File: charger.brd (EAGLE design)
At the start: 42 x 13.2 mm, 12 parts

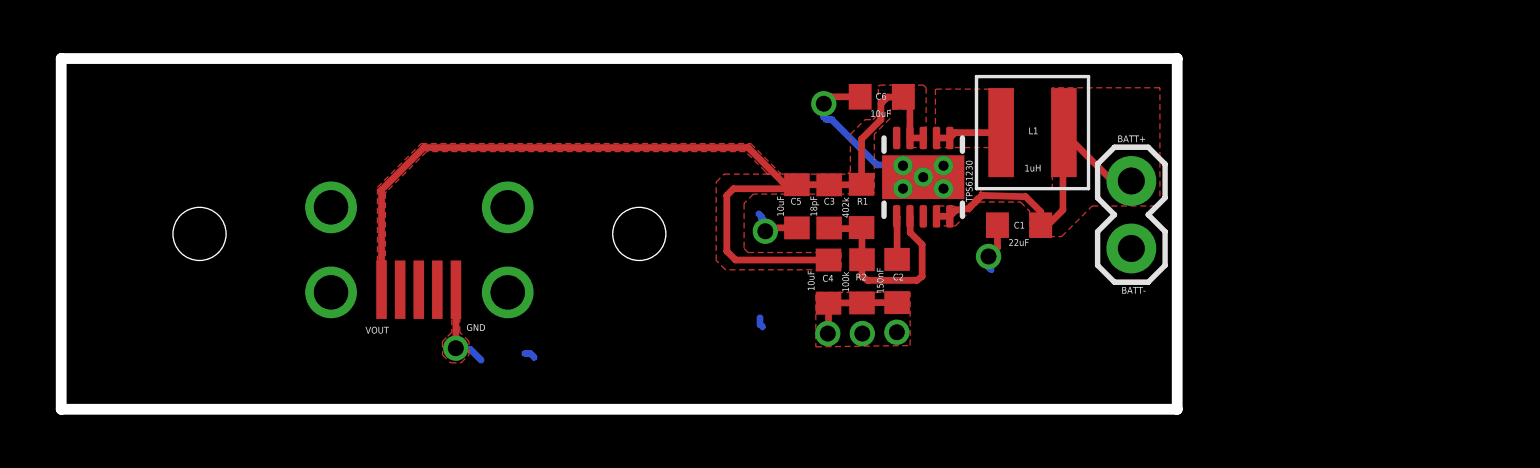
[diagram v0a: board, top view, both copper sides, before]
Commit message: Fixed inductor footprint, updated layout
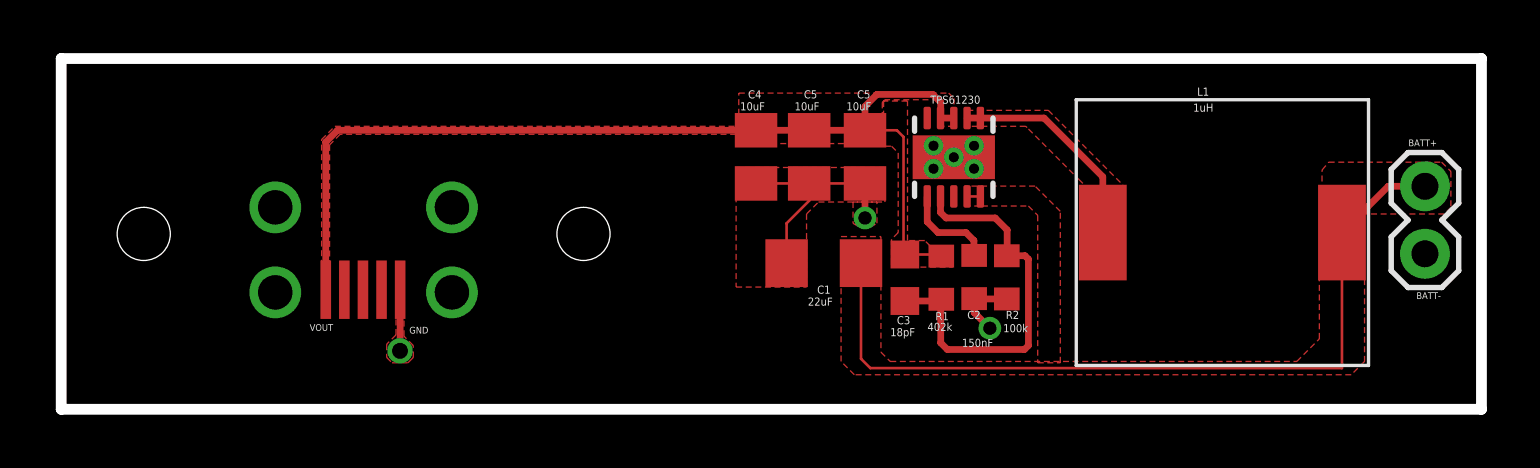
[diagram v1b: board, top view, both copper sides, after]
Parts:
- removed L1: 1uH, Coilcraft:XFL4020
- added U$3: SRU1028, ti:SRU1028
- C1: device adafruit:C0603K -> resistor:C1206
- C3: value 18pF -> 18 pF; device adafruit:C0603K -> resistor:C0603K
- C4, C5, C6: device adafruit:C0603K -> resistor:C0805K
- moved JP1 11.1 mm to (51.3, 5.85)
- moved C1 7.49 mm to (28.7, 5.50)
- moved R2 5.45 mm to (35.6, 4.97)
- moved C4 5.43 mm to (26.1, 9.50)
- moved R1 4.04 mm to (33.1, 4.95)
- moved C3 3.92 mm to (31.8, 4.95)
- moved C2 2.90 mm to (34.4, 4.98)
- moved C6 2.35 mm to (30.2, 9.50), turned to 270 degrees
- moved U$2 2.10 mm to (3.11, 6.60)
- moved C5 1.92 mm to (28.1, 9.50)
- moved U$1 1.37 mm to (33.6, 9.49)
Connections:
- net IND: now also U$3.P$2; no longer L1.P$2
- net VIN: now also U$3.P$1; no longer L1.P$1
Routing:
- net VIN: track 12.3 -> 31.3 mm
- net N$6: track 7.90 -> 15.0 mm
- net IND: track 2.52 -> 8.12 mm
- net GND: track 18.5 -> 16.5 mm, vias 7 -> 3
- net N$3: track 1.63 -> 3.57 mm
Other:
- board size 42 x 13.2 mm -> 53.5 x 13.2 mm
- board text removed: "C6"

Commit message: Fixed dimensions and updated USB connector
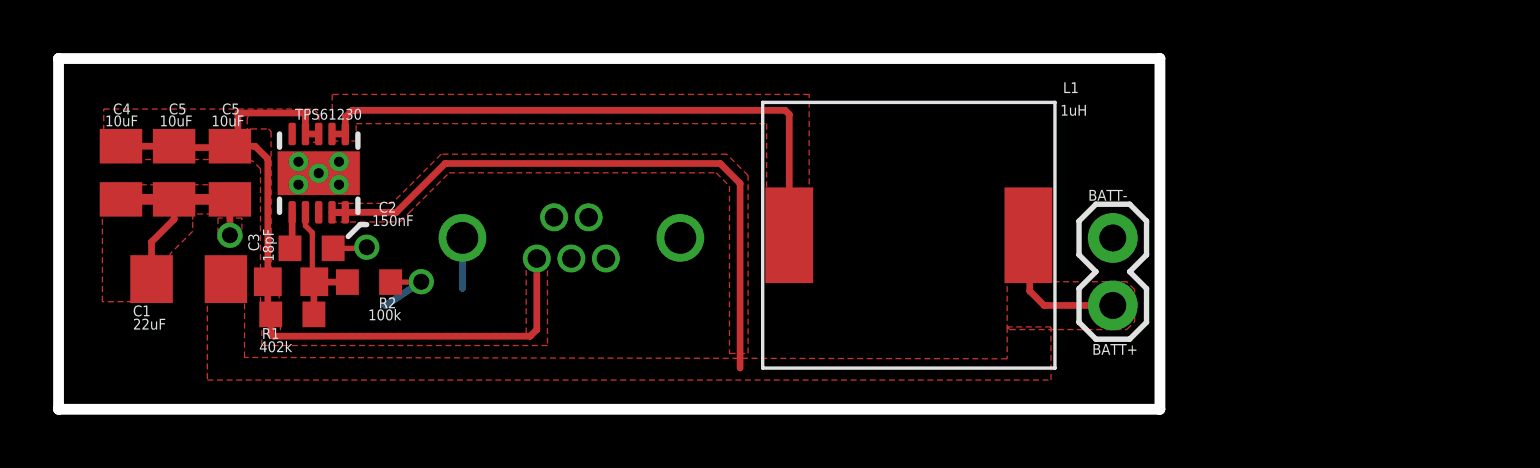
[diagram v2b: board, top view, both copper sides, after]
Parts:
- removed U$2: USB-VERT, ti:USB-VERT
- added U$4: USB2, ti:USB2
- moved C2 25.0 mm to (9.42, 6.06), turned to 0 degrees
- moved R1 24.5 mm to (8.70, 3.57), turned to 180 degrees
- moved R2 24.0 mm to (11.6, 4.79), turned to 180 degrees
- moved C1 23.9 mm to (4.80, 4.90)
- moved C4 23.9 mm to (2.25, 8.90)
- moved C5 23.9 mm to (4.25, 8.90)
- moved C6 23.9 mm to (6.35, 8.90)
- moved U$1 23.9 mm to (9.69, 8.89)
- moved C3 23.1 mm to (8.65, 4.80), turned to 0 degrees
- moved U$3 11.8 mm to (37.3, 8.35)
- moved JP1 11.8 mm to (39.6, 6.45), turned to 270 degrees
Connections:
- net GND: now also U$4.5, U$4.SHIELD1, U$4.SHIELD2; no longer U$2.5
- net VOUT: now also U$4.1; no longer U$2.1
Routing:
- net IND: track 8.12 -> 22.6 mm
- net N$6: track 15.0 -> 6.31 mm
- net VOUT: track 38.6 -> 30.7 mm
- net N$3: track 3.57 -> 1.37 mm
- net VIN: track 31.3 -> 29.4 mm
- net GND: track 16.5 -> 16.0 mm
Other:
- board size 53.5 x 13.2 mm -> 41.5 x 13.2 mm
- board text removed: "GND"
- board text removed: "VOUT"

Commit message: Centered connector, changed length back to 52mm
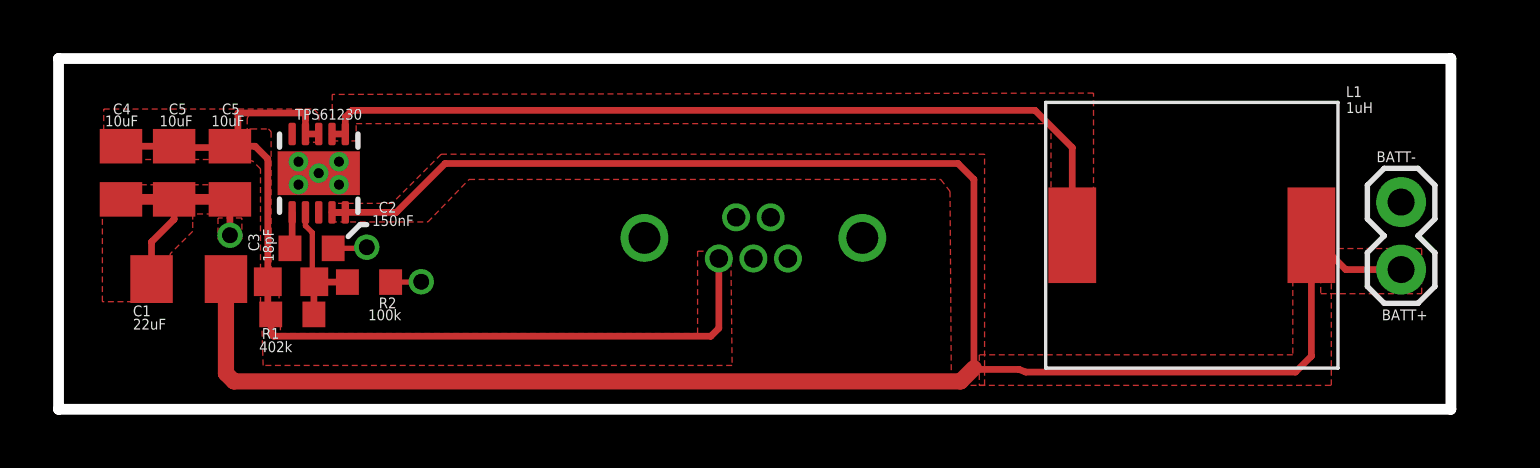
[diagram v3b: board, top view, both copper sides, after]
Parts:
- moved JP1 10.9 mm to (50.4, 7.80)
- moved U$3 10.7 mm to (48.0, 8.35)
- moved U$4 6.85 mm to (21.9, 6.45)
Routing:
- net VIN: track 29.4 -> 86.2 mm
- net IND: track 22.6 -> 32.5 mm
- net VOUT: track 30.7 -> 37.5 mm
- net GND: track 16.0 -> 12.3 mm
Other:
- board size 41.5 x 13.2 mm -> 52.4 x 13.2 mm
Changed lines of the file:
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@@
 <plain>
 <wire x1="-0.1" y1="0" x2="-0.1" y2="13.2" width="0.4064" layer="20"/>
-<wire x1="-0.1" y1="13.2" x2="41.35" y2="13.2" width="0.4064" layer="20"/>
-<wire x1="41.35" y1="13.2" x2="41.35" y2="0" width="0.4064" layer="20"/>
-<wire x1="41.35" y1="0" x2="-0.1" y2="0" width="0.4064" layer="20"/>
-<text x="38.8" y="2.05" size="0.4064" layer="25">BATT+</text>
-<text x="38.65" y="7.85" size="0.4064" layer="25">BATT-</text>
-<text x="37.7" y="11.9" size="0.4064" layer="25">L1</text>
+<wire x1="-0.1" y1="13.2" x2="52.3" y2="13.2" width="0.4064" layer="20"/>
+<wire x1="52.3" y1="13.2" x2="52.3" y2="0" width="0.4064" layer="20"/>
+<wire x1="52.3" y1="0" x2="-0.1" y2="0" width="0.4064" layer="20"/>
+<text x="49.7" y="3.35" size="0.4064" layer="25">BATT+</text>
+<text x="49.5" y="9.3" size="0.4064" layer="25">BATT-</text>
+<text x="48.35" y="11.75" size="0.4064" layer="25">L1</text>
 <text x="8.8" y="10.9" size="0.4064" layer="25">TPS61230</text>
 <text x="1.95" y="11.1" size="0.4064" layer="25">C4</text>
@@
 <text x="11.7" y="6.9" size="0.4064" layer="25">150nF</text>
 <text x="11.55" y="3.35" size="0.4064" layer="25">100k</text>
-<text x="37.6" y="11.05" size="0.4064" layer="25">1uH</text>
+<text x="48.35" y="11.15" size="0.4064" layer="25">1uH</text>
 <wire x1="11.5" y1="6.95" x2="11.25" y2="6.95" width="0.2" layer="25"/>
 <wire x1="11.25" y1="6.95" x2="10.8" y2="6.5" width="0.2" layer="25"/>
@@
 <attribute name="VALUE" x="12.4732" y="6.819" size="1.27" layer="27" rot="R180"/>
 </element>
-<element name="JP1" library="SparkFun-Connectors" package="1X02" value="M02PTH" x="39.576" y="6.448" smashed="yes" rot="R270">
-<attribute name="VALUE" x="36.401" y="7.718" size="1.27" layer="27" rot="R270"/>
-</element>
-<element name="U$3" library="ti" package="SRU1028" value="SRU1028" x="37.3" y="8.35" rot="R180"/>
+<element name="JP1" library="SparkFun-Connectors" package="1X02" value="M02PTH" x="50.426" y="7.798" smashed="yes" rot="R270">
+<attribute name="VALUE" x="47.251" y="9.068" size="1.27" layer="27" rot="R270"/>
+</element>
+<element name="U$3" library="ti" package="SRU1028" value="SRU1028" x="47.95" y="8.35" rot="R180"/>
 <element name="C3" library="resistor" package="C0603K" value="18 pF" x="8.65" y="4.8" smashed="yes">
 <attribute name="VALUE" x="7.85" y="3.15" size="1.016" layer="27"/>
@@
 <attribute name="VALUE" x="0.35" y="9.9" size="1.016" layer="27" rot="R270"/>
 </element>
-<element name="U$4" library="ti" package="USB2" value="USB2" x="15.1" y="6.45"/>
+<element name="U$4" library="ti" package="USB2" value="USB2" x="21.95" y="6.45"/>
 </elements>
 <signals>
@@
 <wire x1="10.692" y1="10.3606" x2="10.692" y2="10.992" width="0.254" layer="1"/>
 <wire x1="10.692" y1="10.992" x2="10.95" y2="11.25" width="0.254" layer="1"/>
-<wire x1="10.95" y1="11.25" x2="27.25" y2="11.25" width="0.254" layer="1"/>
-<wire x1="27.4" y1="11.1" x2="27.4" y2="6.55" width="0.254" layer="1"/>
-<wire x1="27.25" y1="11.25" x2="27.4" y2="11.1" width="0.254" layer="1"/>
+<wire x1="10.95" y1="11.25" x2="36.65" y2="11.25" width="0.254" layer="1"/>
 <polygon width="0.254" layer="1" thermals="no">
-<vertex x="26.55" y="4.85"/>
-<vertex x="28.15" y="4.85"/>
-<vertex x="28.15" y="11.85"/>
+<vertex x="37.25" y="4.85"/>
+<vertex x="38.85" y="4.9"/>
+<vertex x="38.85" y="11.9"/>
 <vertex x="10.2" y="11.85"/>
 <vertex x="10.2" y="10.1"/>
-<vertex x="11" y="10.1"/>
 <vertex x="11.1" y="10.1"/>
 <vertex x="11.1" y="10.75"/>
-<vertex x="26.55" y="10.75"/>
-</polygon>
+<vertex x="37.25" y="10.75"/>
+</polygon>
+<wire x1="36.65" y1="11.25" x2="38.05" y2="9.85" width="0.254" layer="1"/>
+<wire x1="38.05" y1="9.85" x2="38.05" y2="6.55" width="0.254" layer="1"/>
 </signal>
 <signal name="VIN">
@@
 <contactref element="U$3" pad="P$1"/>
 <contactref element="C1" pad="1"/>
-<wire x1="39.576" y1="3.908" x2="36.992" y2="3.908" width="0.254" layer="1"/>
-<wire x1="36.992" y1="3.908" x2="36.45" y2="4.45" width="0.254" layer="1"/>
-<wire x1="36.45" y1="4.45" x2="36.45" y2="6.5" width="0.254" layer="1"/>
-<wire x1="36.45" y1="6.5" x2="36.4" y2="6.55" width="0.254" layer="1"/>
-<polygon width="0.254" layer="1" thermals="no">
-<vertex x="35.6" y="8.25"/>
-<vertex x="35.6" y="3.1"/>
-<vertex x="35.7" y="3"/>
-<vertex x="40.1" y="3"/>
-<vertex x="40.4" y="3.3"/>
-<vertex x="40.4" y="4.5"/>
-<vertex x="40.1" y="4.8"/>
-<vertex x="37.2" y="4.8"/>
-<vertex x="37.2" y="8.25"/>
-</polygon>
-<polygon width="0.254" layer="1" thermals="no">
-<vertex x="5.5" y="5.7"/>
-<vertex x="5.5" y="1.1"/>
-<vertex x="37.25" y="1.1"/>
-<vertex x="37.25" y="3.1"/>
-<vertex x="35.6" y="3.1"/>
-<vertex x="35.6" y="1.9"/>
-<vertex x="6.9" y="1.95"/>
-<vertex x="6.9" y="5.7"/>
-</polygon>
 <wire x1="10.192" y1="7.4106" x2="10.692" y2="7.4106" width="0.254" layer="1"/>
-<wire x1="10.192" y1="7.4106" x2="12.6106" y2="7.4106" width="0.254" layer="1"/>
-<wire x1="12.6106" y1="7.4106" x2="14.45" y2="9.25" width="0.254" layer="1"/>
-<wire x1="14.45" y1="9.25" x2="24.8" y2="9.25" width="0.254" layer="1"/>
-<wire x1="24.8" y1="9.25" x2="25.55" y2="8.5" width="0.254" layer="1"/>
-<wire x1="25.55" y1="8.5" x2="25.55" y2="1.55" width="0.254" layer="1"/>
 <polygon width="0.2" layer="1" thermals="no">
 <vertex x="10.15" y="7.75"/>
 <vertex x="10.15" y="7.05"/>
-<vertex x="12.75" y="7.05"/>
-<vertex x="13.1" y="7.4"/>
-<vertex x="14.6" y="8.9"/>
-<vertex x="24.65" y="8.9"/>
-<vertex x="25.15" y="8.4"/>
-<vertex x="25.15" y="2.1"/>
-<vertex x="25.85" y="2.1"/>
-<vertex x="25.85" y="8.8"/>
-<vertex x="25.05" y="9.6"/>
+<vertex x="13.8" y="7.05"/>
+<vertex x="15.35" y="8.65"/>
+<vertex x="33.1" y="8.65"/>
+<vertex x="33.45" y="8.2"/>
+<vertex x="33.5" y="0.9"/>
+<vertex x="34.75" y="0.9"/>
+<vertex x="34.75" y="9.6"/>
 <vertex x="14.3" y="9.6"/>
 <vertex x="12.45" y="7.75"/>
+</polygon>
+<wire x1="50.426" y1="5.258" x2="48.342" y2="5.258" width="0.254" layer="1"/>
+<wire x1="48.342" y1="5.258" x2="47.05" y2="6.55" width="0.254" layer="1"/>
+<wire x1="47.05" y1="6.55" x2="47.05" y2="2" width="0.254" layer="1"/>
+<wire x1="47.05" y1="2" x2="46.45" y2="1.4" width="0.254" layer="1"/>
+<wire x1="46.45" y1="1.4" x2="36.3" y2="1.4" width="0.254" layer="1"/>
+<wire x1="10.192" y1="7.4106" x2="12.6106" y2="7.4106" width="0.254" layer="1"/>
+<wire x1="12.6106" y1="7.4106" x2="14.45" y2="9.25" width="0.254" layer="1"/>
+<wire x1="14.45" y1="9.25" x2="33.75" y2="9.25" width="0.254" layer="1"/>
+<wire x1="33.75" y1="9.25" x2="34.35" y2="8.65" width="0.254" layer="1"/>
+<wire x1="34.35" y1="8.65" x2="34.35" y2="1.55" width="0.254" layer="1"/>
+<wire x1="34.35" y1="1.55" x2="34.4" y2="1.5" width="0.254" layer="1"/>
+<wire x1="34.4" y1="1.5" x2="36.05" y2="1.5" width="0.254" layer="1"/>
+<wire x1="36.05" y1="1.5" x2="36.3" y2="1.4" width="0.254" layer="1"/>
+<polygon width="0.254" layer="1" thermals="no">
+<vertex x="50.8" y="6.05"/>
+<vertex x="47.4" y="6.05"/>
+<vertex x="47.4" y="4.35"/>
+<vertex x="51.2" y="4.35"/>
+<vertex x="51.2" y="6.05"/>
+</polygon>
+<wire x1="6.2" y1="4.9" x2="6.2" y2="1.35" width="0.6096" layer="1"/>
+<wire x1="6.2" y1="1.35" x2="6.5" y2="1.05" width="0.6096" layer="1"/>
+<wire x1="6.5" y1="1.05" x2="33.85" y2="1.05" width="0.6096" layer="1"/>
+<wire x1="33.85" y1="1.05" x2="34.35" y2="1.55" width="0.6096" layer="1"/>
+<polygon width="0.3048" layer="1" thermals="no">
+<vertex x="46.35" y="4.85"/>
+<vertex x="46.35" y="2.05"/>
+<vertex x="34.55" y="2.05"/>
+<vertex x="34.55" y="0.9"/>
+<vertex x="47.8" y="0.9"/>
+<vertex x="47.8" y="4.9"/>
+<vertex x="46.35" y="4.9"/>
 </polygon>
 </signal>
@@
 <polygon width="0.4064" layer="16">
 <vertex x="0" y="13.2"/>
-<vertex x="41.35" y="13.2"/>
-<vertex x="41.35" y="0"/>
+<vertex x="52.25" y="13.2"/>
+<vertex x="52.25" y="0"/>
 <vertex x="0" y="0"/>
 </polygon>
@@
 <wire x1="2.25" y1="7.9" x2="4.25" y2="7.9" width="0.4064" layer="1"/>
 <wire x1="4.25" y1="7.9" x2="6.35" y2="7.9" width="0.4064" layer="1"/>
-<wire x1="15.1" y1="6.45" x2="15.1" y2="4.55" width="0.254" layer="16"/>
 <wire x1="6.35" y1="7.9" x2="6.35" y2="6.55" width="0.254" layer="1"/>
 <via x="6.35" y="6.55" extent="1-16" drill="0.6"/>
@@
 <wire x1="9.2602" y1="9.3174" x2="9.692" y2="8.8856" width="0.254" layer="1"/>
 <via x="11.5" y="6.1" extent="1-16" drill="0.6"/>
-<wire x1="11.5" y1="6.1" x2="11.4" y2="6.15" width="0.254" layer="16"/>
-<wire x1="11.4" y1="6.15" x2="11.45" y2="6.2" width="0.254" layer="16"/>
 <via x="13.55" y="4.8" extent="1-16" drill="0.6"/>
-<wire x1="13.55" y1="4.8" x2="12.2" y2="3.9" width="0.254" layer="16"/>
 <wire x1="12.397" y1="4.787" x2="13.437" y2="4.787" width="0.2" layer="1"/>
 <wire x1="13.437" y1="4.787" x2="13.55" y2="4.8" width="0.2" layer="1"/>
@@
 <wire x1="7.775" y1="4.8" x2="7.775" y2="3.7306" width="0.254" layer="1"/>
 <wire x1="7.775" y1="3.7306" x2="7.8846" y2="3.571" width="0.254" layer="1"/>
-<wire x1="17.9" y1="5.675" x2="17.9" y2="3" width="0.254" layer="1"/>
-<wire x1="17.9" y1="3" x2="17.65" y2="2.75" width="0.254" layer="1"/>
-<wire x1="17.65" y1="2.75" x2="8" y2="2.75" width="0.254" layer="1"/>
+<wire x1="24.45" y1="2.75" x2="8" y2="2.75" width="0.254" layer="1"/>
 <wire x1="8" y1="2.75" x2="7.9" y2="2.85" width="0.254" layer="1"/>
 <wire x1="7.9" y1="2.85" x2="7.9" y2="3.6056" width="0.254" layer="1"/>
@@
 <vertex x="8.25" y="3.2"/>
 <vertex x="8.25" y="2.85"/>
-<vertex x="17.5" y="2.85"/>
-<vertex x="17.5" y="5.95"/>
-<vertex x="18.3" y="5.95"/>
-<vertex x="18.3" y="2.4"/>
-<vertex x="7.55" y="2.4"/>
+<vertex x="23.95" y="2.85"/>
+<vertex x="23.95" y="5.95"/>
+<vertex x="25.2" y="5.95"/>
+<vertex x="25.25" y="1.65"/>
+<vertex x="7.6" y="1.65"/>
 <vertex x="7.55" y="3.2"/>
 </polygon>
+<wire x1="24.45" y1="2.75" x2="24.75" y2="3.05" width="0.254" layer="1"/>
+<wire x1="24.75" y1="3.05" x2="24.75" y2="5.675" width="0.254" layer="1"/>
 </signal>
 <signal name="N$6">
